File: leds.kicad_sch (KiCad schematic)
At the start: 6 parts, among them J15 Conn_01x02, J16 Conn_01x02, J17 Conn_01x02, J18 Conn_01x02, U1 TC4427, U2 TC4427

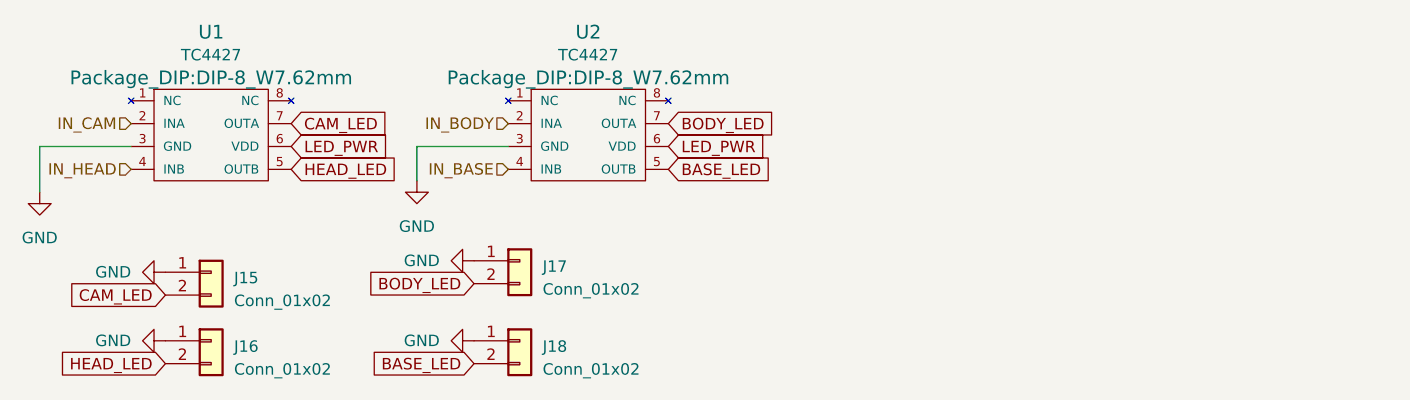
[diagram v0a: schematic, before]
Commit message: Redesign for SMD and new pinmap
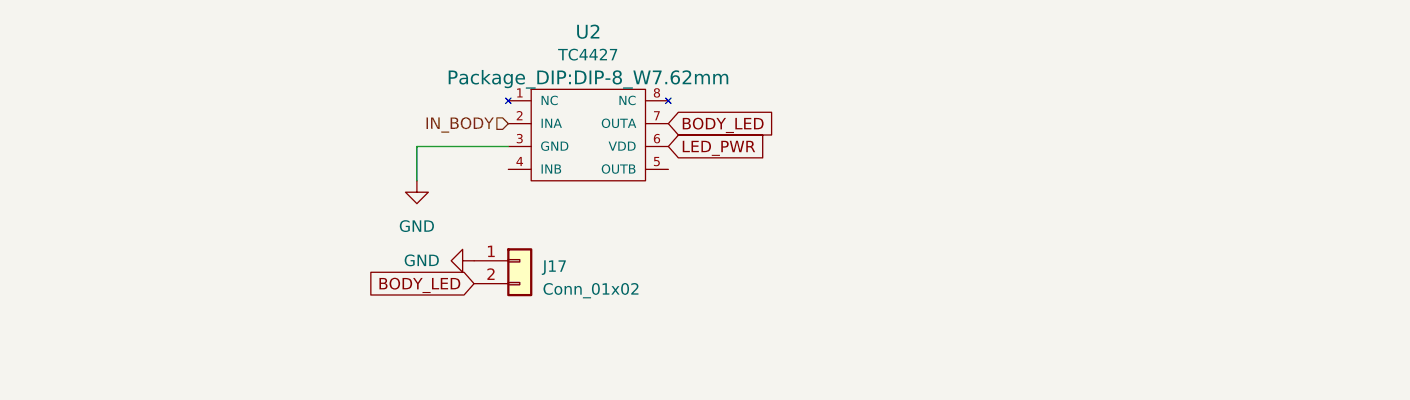
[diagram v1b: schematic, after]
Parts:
- removed J15, J16, J18: Conn_01x02, Connector_JST:JST_XH_B2B-XH-A_1x02_P2.50mm_Vertical, symbol Connector_Generic:Conn_01x02
- removed U1: TC4427, Package_DIP:DIP-8_W7.62mm, symbol Driver_FET2:TC4427
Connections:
- net BASE_LED: no longer names the net of U2.5 (OUTB)
- net IN_BASE: no longer names the net of U2.4 (INB)

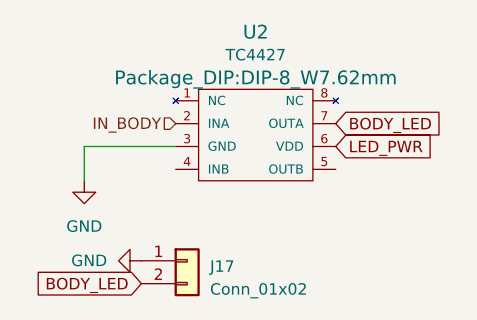
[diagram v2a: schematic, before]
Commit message: Fix global labels
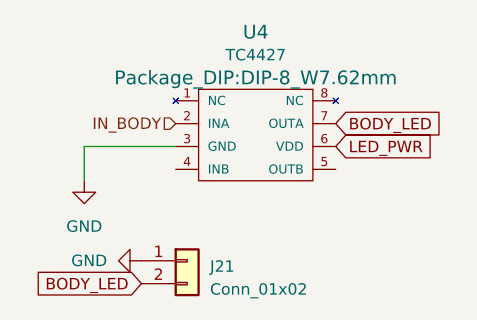
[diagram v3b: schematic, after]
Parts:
- renumbered J17 to J21, U2 to U4
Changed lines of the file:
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@@
 		(dnp no)
 		(fields_autoplaced yes)
-		(property "Reference" "J17"
+		(property "Reference" "J21"
 			(at 165.1 102.235 0)
 			(effects
@@
 			(project "P2 Kevinbot Board"
 				(path "/362ca48c-0b77-4943-b8b3-fc15ab97f30d/971de258-84b3-438c-84b6-ee44796701a6"
-					(reference "J17")
+					(reference "J21")
 					(unit 1)
 				)
@@
 		(on_board yes)
 		(dnp no)
-		(property "Reference" "U2"
+		(property "Reference" "U4"
 			(at 170.18 76.2 0)
 			(effects
@@
 			(project "P2 Kevinbot Board"
 				(path "/362ca48c-0b77-4943-b8b3-fc15ab97f30d/971de258-84b3-438c-84b6-ee44796701a6"
-					(reference "U2")
+					(reference "U4")
 					(unit 1)
 				)
@@
 		(dnp no)
 		(fields_autoplaced yes)
-		(property "Reference" "#PWR036"
+		(property "Reference" "#PWR055"
 			(at 151.13 99.06 0)
 			(effects
@@
 			(project "P2 Kevinbot Board"
 				(path "/362ca48c-0b77-4943-b8b3-fc15ab97f30d/971de258-84b3-438c-84b6-ee44796701a6"
-					(reference "#PWR036")
+					(reference "#PWR055")
 					(unit 1)
 				)
@@
 		(dnp no)
 		(fields_autoplaced yes)
-		(property "Reference" "#PWR037"
+		(property "Reference" "#PWR056"
 			(at 151.13 101.6 0)
 			(effects
@@
 			(project "P2 Kevinbot Board"
 				(path "/362ca48c-0b77-4943-b8b3-fc15ab97f30d/971de258-84b3-438c-84b6-ee44796701a6"
-					(reference "#PWR037")
-					(unit 1)
-				)
+					(reference "#PWR056")
+					(unit 1)
+				)

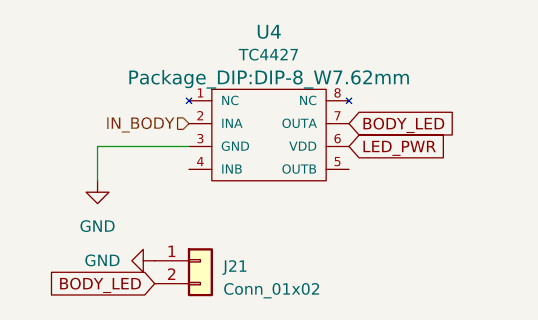
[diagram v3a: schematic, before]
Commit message: Add new kevinbot logo
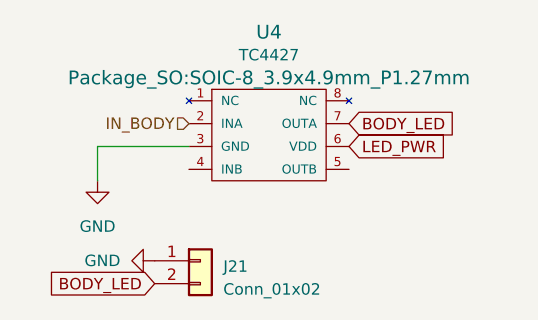
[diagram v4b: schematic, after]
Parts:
- U4: footprint Package_DIP:DIP-8_W7.62mm -> Package_SO:SOIC-8_3.9x4.9mm_P1.27mm
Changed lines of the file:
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@@
 			)
 		)
-		(property "Footprint" "Package_DIP:DIP-8_W7.62mm"
+		(property "Footprint" "Package_SO:SOIC-8_3.9x4.9mm_P1.27mm"
 			(at 170.18 81.28 0)
 			(effects

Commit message: DRC fixes, add missing library, misc
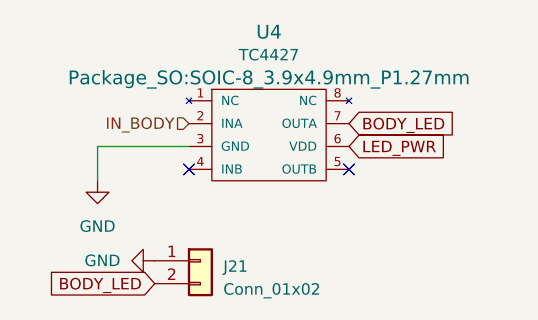
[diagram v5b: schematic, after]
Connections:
- no-connect marks 0 -> 2
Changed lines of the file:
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@@
 	(generator_version "8.0")
 	(paper "A4")
+	(no_connect
+		(at 179.07 91.44)
+	)
+	(no_connect
+		(at 161.29 91.44)
+	)
 	(wire
 		(pts
@@
 		(at 162.56 101.6 0)
 		(unit 1)
-		(exclude_from_sim no)
+		(exclude_from_sim yes)
 		(in_bom yes)
 		(on_board yes)
@@
 			)
 		)
-		(property "Description" ""
+		(property "Description" "Generic connector, single row, 01x02, script generated (kicad-library-utils/schlib/autogen/connector/)"
 			(at 162.56 101.6 0)
 			(effects
@@
 		(at 170.18 87.63 0)
 		(unit 1)
-		(exclude_from_sim no)
+		(exclude_from_sim yes)
 		(in_bom yes)
 		(on_board yes)
@@
 			)
 		)
-		(property "Description" ""
+		(property "Description" "Power symbol creates a global label with name \"GND\" , ground"
 			(at 151.13 92.71 0)
 			(effects
@@
 			)
 		)
-		(property "Description" ""
+		(property "Description" "Power symbol creates a global label with name \"GND\" , ground"
 			(at 157.48 101.6 0)
 			(effects

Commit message: Add mfr part numbers and datasheets to all
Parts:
- J21: Part Number (none) -> B2B-XH-A
- U4: Part Number (none) -> TC4427ACOA713
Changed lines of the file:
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@@
 			)
 		)
-		(property "Datasheet" "~"
+		(property "Datasheet" "https://www.jst-mfg.com/product/pdf/eng/eXH.pdf"
 			(at 162.56 101.6 0)
 			(effects
@@
 		)
 		(property "Description" "Generic connector, single row, 01x02, script generated (kicad-library-utils/schlib/autogen/connector/)"
+			(at 162.56 101.6 0)
+			(effects
+				(font
+					(size 1.27 1.27)
+				)
+				(hide yes)
+			)
+		)
+		(property "Part Number" "B2B-XH-A"
 			(at 162.56 101.6 0)
 			(effects
@@
 			)
 		)
-		(property "Datasheet" ""
-			(at 170.18 87.63 0)
+		(property "Datasheet" "https://ww1.microchip.com/downloads/en/DeviceDoc/20001423J.pdf"
+			(at 169.672 70.866 0)
 			(effects
 				(font
 					(size 1.524 1.524)
 				)
+				(hide yes)
 			)
 		)
@@
 			(at 170.18 87.63 0)
 			(effects
+				(font
+					(size 1.27 1.27)
+				)
+				(hide yes)
+			)
+		)
+		(property "Part Number" "TC4427ACOA713"
+			(at 170.18 87.63 0)
+			(effects

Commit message: Add rsl
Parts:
- added J32: Conn_01x02, Connector_JST:JST_XH_B2B-XH-A_1x02_P2.50mm_Vertical, symbol Connector_Generic:Conn_01x02
- added Q2: IRLML6402, Package_TO_SOT_SMD:SOT-23, symbol Transistor_FET:IRLML6402
- added R26: 680R, Resistor_SMD:R_0603_1608Metric, symbol Device:R
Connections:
- net BODY_LED: now also J21.1 (Pin_1); no longer J21.2 (Pin_2)
- net GND: now also J21.2 (Pin_2), Q2.2 (S); no longer J21.1 (Pin_1)
- net LED_PWR: now also J32.1 (Pin_1)
- new net: Q2.1 (G), R26.2
- new net: J32.2 (Pin_2), Q2.3 (D)
- new net IN_RSL: R26.1

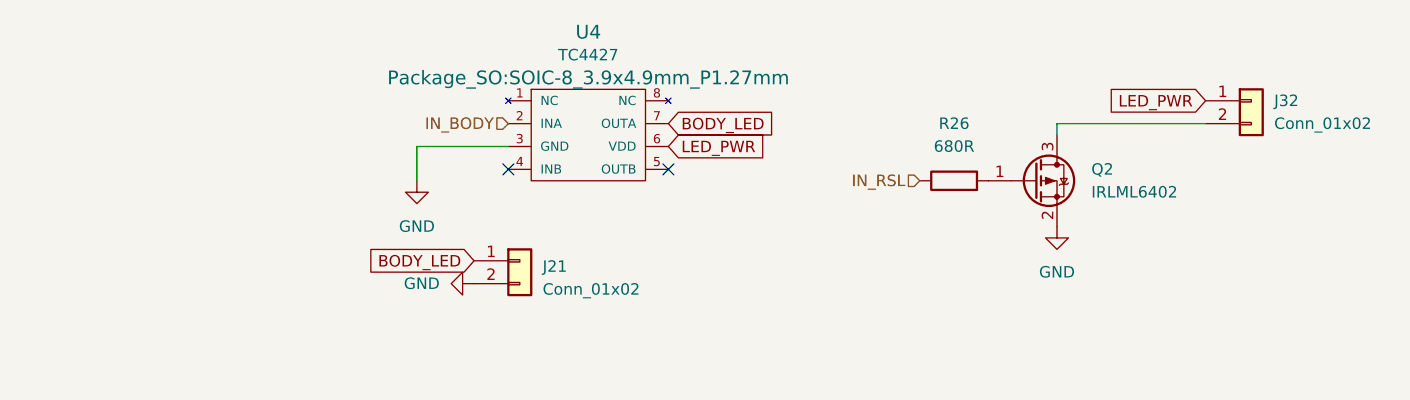
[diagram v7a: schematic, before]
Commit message: Silkscreen changes, DRC, make ground pin 1 for more conns
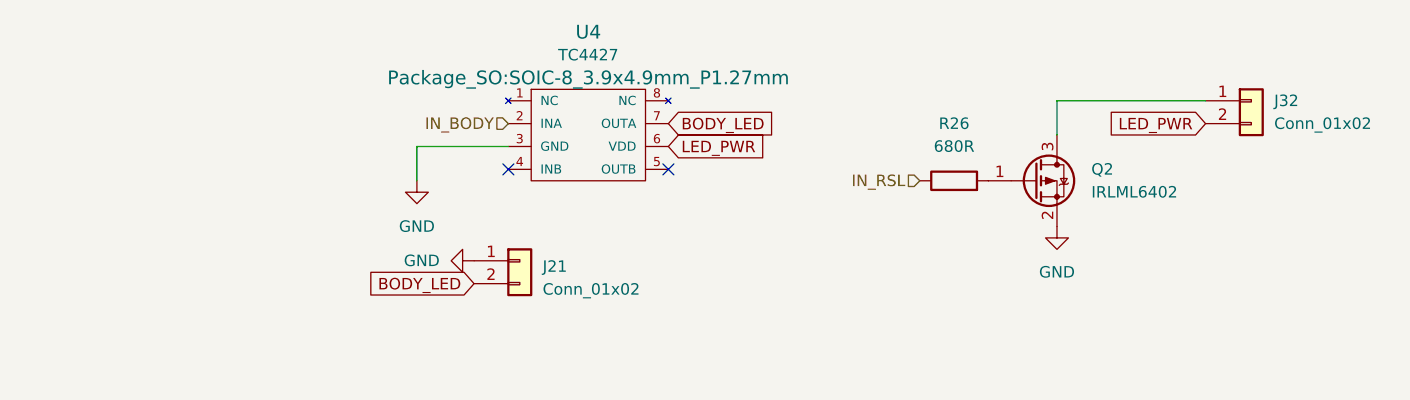
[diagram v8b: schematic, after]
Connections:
- net BODY_LED: now also J21.2 (Pin_2); no longer J21.1 (Pin_1)
- net GND: now also J21.1 (Pin_1); no longer J21.2 (Pin_2)
- net LED_PWR: now also J32.2 (Pin_2); no longer J32.1 (Pin_1)
- net at Q2.3 (D): now also J32.1 (Pin_1); no longer J32.2 (Pin_2)
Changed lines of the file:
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@@
+	(wire
+		(pts
+			(xy 222.25 83.82) (xy 238.76 83.82)
+		)
+		(stroke
+			(width 0)
+			(type default)
+		)
+	)
 	(wire
 		(pts
@@
 	(wire
 		(pts
-			(xy 222.25 86.36) (xy 222.25 87.63)
+			(xy 222.25 83.82) (xy 222.25 87.63)
 		)
 		(stroke
@@
 		)
 	)
-	(wire
-		(pts
-			(xy 238.76 86.36) (xy 222.25 86.36)
-		)
-		(stroke
-			(width 0)
-			(type default)
-		)
-	)
 	(global_label "BODY_LED"
 		(shape input)
-		(at 157.48 101.6 180)
+		(at 157.48 104.14 180)
 		(fields_autoplaced yes)
 		(effects
@@
 		)
 		(property "Intersheetrefs" "${INTERSHEET_REFS}"
-			(at 145.6931 101.6794 0)
+			(at 145.6931 104.2194 0)
 			(effects
 				(font
@@
 	(global_label "LED_PWR"
 		(shape input)
-		(at 238.76 83.82 180)
+		(at 238.76 86.36 180)
 		(fields_autoplaced yes)
 		(effects
@@
 		)
 		(property "Intersheetrefs" "${INTERSHEET_REFS}"
-			(at 227.3687 83.82 0)
+			(at 227.3687 86.36 0)
 			(effects
 				(font
@@
 	(symbol
 		(lib_id "power:GND")
-		(at 157.48 104.14 270)
+		(at 157.48 101.6 270)
 		(unit 1)
 		(exclude_from_sim no)
@@
 		(fields_autoplaced yes)
 		(property "Reference" "#PWR056"
-			(at 151.13 104.14 0)
+			(at 151.13 101.6 0)
 			(effects
 				(font
@@
 		)
 		(property "Value" "GND"
-			(at 153.67 104.1399 90)
+			(at 153.67 101.5999 90)
 			(effects
 				(font
@@
 		)
 		(property "Footprint" ""
-			(at 157.48 104.14 0)
+			(at 157.48 101.6 0)
 			(effects
 				(font
@@
 		)
 		(property "Datasheet" ""
-			(at 157.48 104.14 0)
+			(at 157.48 101.6 0)
 			(effects
 				(font
@@
 		)
 		(property "Description" "Power symbol creates a global label with name \"GND\" , ground"
-			(at 157.48 104.14 0)
-			(effects
-				(font
+			(at 157.48 101.6 0)
+			(effects
+				(font
